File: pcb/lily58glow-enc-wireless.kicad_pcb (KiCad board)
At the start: 2 copper layers, 142.5 x 106.3 mm, 120 parts, among them J1 LED, J2 4PIN, P1 i2c_pin, P2 i2c_pin, P3 ICSP, P4 OLED, SW1 SW_PUSH, SW10 SW_PUSH, SW11 SW_PUSH, SW12 SW_PUSH, SW13 SW_PUSH, SW14 SW_PUSH, SW15 SW_PUSH, SW16 SW_PUSH, SW17 SW_PUSH, SW18 SW_PUSH, SW19 SW_PUSH, SW2 SW_PUSH, SW20 SW_PUSH, SW21 SW_PUSH, SW22 SW_PUSH, SW23 SW_PUSH, SW24 SW_PUSH, SW25 Rotary_Encoder_Switch, SW26 SW_PUSH, SW27 SW_PUSH, SW28 SW_PUSH, SW29 SW_PUSH, SW3 SW_PUSH, SW4 SW_PUSH, SW5 SW_PUSH, SW6 SW_PUSH, SW7 SW_PUSH, SW8 SW_PUSH, SW9 SW_PUSH, U1 ProMicro

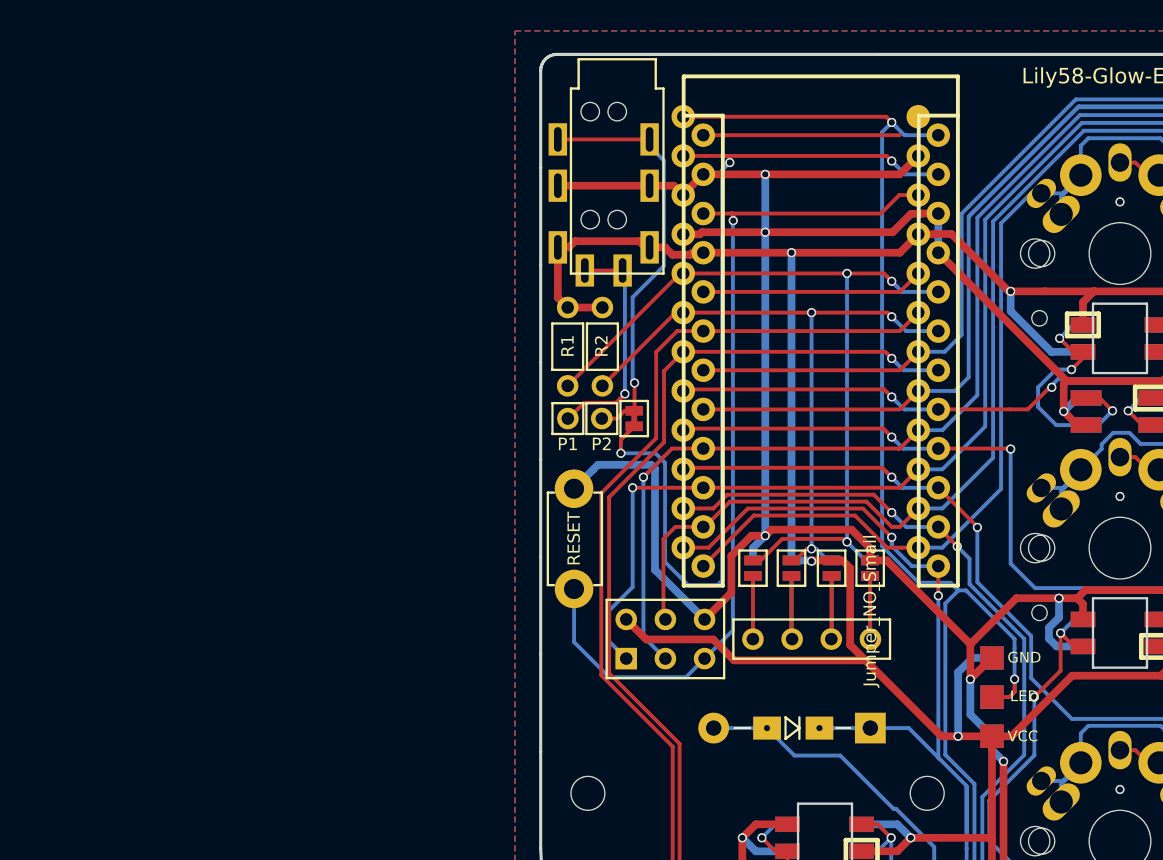
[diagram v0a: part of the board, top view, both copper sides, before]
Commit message: Updates to schematics
Might just scrap all of the traces and start from scratch...
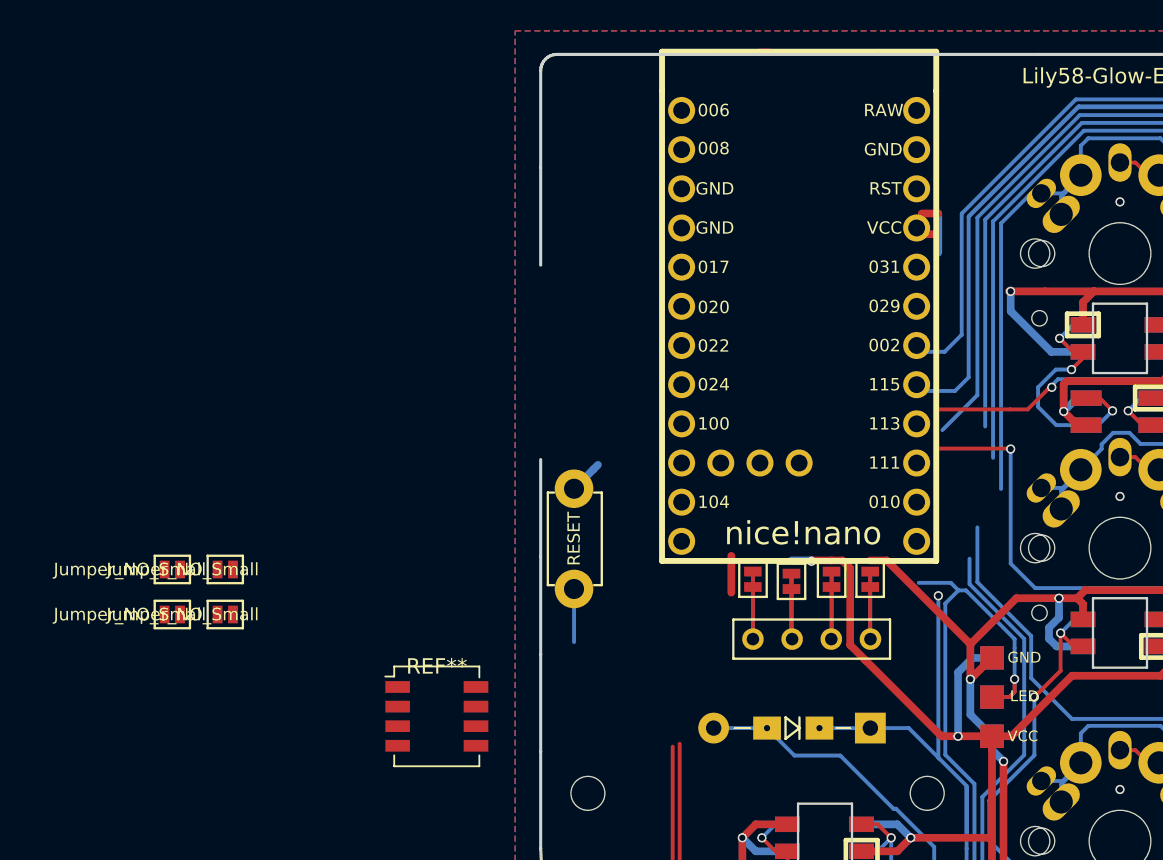
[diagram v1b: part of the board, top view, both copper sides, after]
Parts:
- removed J2: 4PIN, Lily58-footprint:MJ-4PP-9
- removed P1, P2: i2c_pin, Lily58-footprint:1pin_conn
- removed P3: ICSP, Lily58-footprint:ICSP
- removed R1, R2: R, Lily58-footprint:RESISTOR_mini
- removed W1: jumper, Lily58-footprint:jumper_data
- added REF**: SW_DIP_SPSTx04_Slide_Copal_CHS-04A_W5.08mm_P1.27mm_JPin, Button_Switch_SMD:SW_DIP_SPSTx04_Slide_Copal_CHS-04A_W5.08mm_P1.27mm_JPin, F.Cu at (76.2, 80.0)
- JP5, JP6, JP7, JP8: moved to F.Cu
- U1: footprint Lily58-footprint:ProMicro_rev2 -> nice-nano-kicad:nice_nano
- moved JP5 45.2 mm to (59.1, 70.5), turned to 0 degrees
- moved JP6 42.9 mm to (59.1, 73.4), turned to 0 degrees
- moved JP7 36.7 mm to (62.5, 70.5), turned to 0 degrees
- moved JP8 34.3 mm to (62.5, 73.4), turned to 0 degrees
- moved U1 1.78 mm to (99.7, 54.7), turned to -90 degrees
- moved JP3 0.85 mm to (99.2, 71.3)
- moved JP1 0.72 mm to (104.3, 71.1)
- moved JP2 0.72 mm to (101.8, 71.1)
- moved JP4 0.72 mm to (96.7, 71.1)
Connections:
- L1 pad 3: Net-(L1-Pad3) -> Net-(LEDDIP1-Pad8)
- L1 pad 4: VCC -> Net-(L1-Pad4)
- L10 pad 4: VCC -> Net-(L1-Pad4)
- L11 pad 4: VCC -> Net-(L1-Pad4)
- L12 pad 4: VCC -> Net-(L1-Pad4)
- L13 pad 4: VCC -> Net-(L1-Pad4)
- L14 pad 4: VCC -> Net-(L1-Pad4)
- L15 pad 4: VCC -> Net-(L1-Pad4)
- L16 pad 4: VCC -> Net-(L1-Pad4)
- L17 pad 4: VCC -> Net-(L1-Pad4)
- L18 pad 4: VCC -> Net-(L1-Pad4)
- L19 pad 4: VCC -> Net-(L1-Pad4)
- L2 pad 4: VCC -> Net-(L1-Pad4)
- L20 pad 4: VCC -> Net-(L1-Pad4)
- L21 pad 4: VCC -> Net-(L1-Pad4)
- L22 pad 4: VCC -> Net-(L1-Pad4)
- L23 pad 4: VCC -> Net-(L1-Pad4)
- L24 pad 4: VCC -> Net-(L1-Pad4)
- L25 pad 4: VCC -> Net-(L1-Pad4)
- L26 pad 4: VCC -> Net-(L1-Pad4)
- L27 pad 4: VCC -> Net-(L1-Pad4)
- L28 pad 4: VCC -> Net-(L1-Pad4)
- L29 pad 4: VCC -> Net-(L1-Pad4)
- L3 pad 4: VCC -> Net-(L1-Pad4)
- L30 pad 1: Net-(L30-Pad1) -> unconnected-(L30-Pad1)
- L30 pad 4: VCC -> Net-(L1-Pad4)
- L31 pad 1: Net-(L1-Pad3) -> unconnected-(L31-Pad1)
- L31 pad 4: VCC -> Net-(L31-Pad4)
- L32 pad 4: VCC -> Net-(L31-Pad4)
- L33 pad 4: VCC -> Net-(L31-Pad4)
- L34 pad 3: LED -> Net-(L34-Pad3)
- L34 pad 4: VCC -> Net-(L31-Pad4)
- L35 pad 4: VCC -> Net-(L31-Pad4)
- L36 pad 4: VCC -> Net-(L31-Pad4)
- L4 pad 4: VCC -> Net-(L1-Pad4)
- L5 pad 4: VCC -> Net-(L1-Pad4)
- L6 pad 4: VCC -> Net-(L1-Pad4)
- L7 pad 4: VCC -> Net-(L1-Pad4)
- L8 pad 4: VCC -> Net-(L1-Pad4)
- L9 pad 4: VCC -> Net-(L1-Pad4)
- U1 pad 1: LED -> Net-(LEDDIP1-Pad2)
- U1 pad 20: Net-(U1-Pad20) -> unconnected-(U1-Pad20)
- U1 pad 24: Net-(U1-Pad24) -> unconnected-(U1-Pad24)
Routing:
- net VCC: track 1045.9 -> 2.18 mm, vias 44 -> 0
- net Net-(L1-Pad4): track 0.00 -> 971.1 mm, vias 0 -> 43
- net GND: track 1095.1 -> 985.3 mm, vias 73 -> 69
- net DATA: track 60.9 -> 0.00 mm, vias 3 -> 0
- net RESET: track 57.5 -> 3.44 mm, vias 1 -> 0
- net SDA: track 53.7 -> 0.80 mm, vias 3 -> 0
- net LED: track 121.3 -> 71.3 mm, vias 5 -> 4
- net enc2: track 66.1 -> 19.0 mm
- net enc1: track 60.4 -> 14.0 mm, vias 1 -> 0
- net SCL: track 42.8 -> 0.51 mm, vias 3 -> 0
- net col3: track 300.2 -> 263.3 mm, vias 1 -> 0
- net col2: track 314.4 -> 281.4 mm, vias 1 -> 0
- net col4: track 291.3 -> 261.1 mm
- net Net-(J2-Pad3): track 26.7 -> 0.00 mm, vias 1 -> 0
- net col5: track 185.4 -> 162.3 mm
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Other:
- outline, holes or cut-outs redrawn

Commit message: Starting PCB from scratch, and making single sided boards
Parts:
- removed JP5, JP6, JP7, JP8: Jumper_NO_Small, Lily58-footprint:Jumper
- removed REF**: SW_DIP_SPSTx04_Slide_Copal_CHS-04A_W5.08mm_P1.27mm_JPin, Button_Switch_SMD:SW_DIP_SPSTx04_Slide_Copal_CHS-04A_W5.08mm_P1.27mm_JPin
- D1, D10, D11, D12, D13, D14, D15, D16, D17, D18, D19, D2, D20, D21, D22, D23, D24, D25, D27, D28, D29, D3, D4, D5, D6, D7, D8, D9: moved to F.Cu
- moved JP2 252.1 mm to (350.8, 31.4), turned to 0 degrees
- moved D26 238.7 mm to (333.1, 32.1), turned to 0 degrees
- moved L34 223.3 mm to (328.7, 36.5), turned to 0 degrees
- moved TH7 221.2 mm to (319.5, 60.7), turned to 0 degrees
- moved D25 220.5 mm to (316.8, 44.5), turned to 0 degrees
- moved L19 218.7 mm to (328.9, 46.3)
- moved L8 209.3 mm to (345.0, 32.8)
- moved TH2 201.3 mm to (308.8, 70.5)
- moved D27 200.9 mm to (309.3, 55.5), turned to 0 degrees
- moved J1 194.1 mm to (306.0, 69.1), turned to 0 degrees
- moved L2 181.7 mm to (321.1, 49.4), turned to 0 degrees
- moved L31 181.3 mm to (300.6, 81.2)
- moved L27 175.5 mm to (273.5, 102.0), turned to 0 degrees
- moved JP3 175.1 mm to (269.5, 112.0), turned to 0 degrees
- moved RSW1 175.1 mm to (255.3, 109.6), turned to 0 degrees
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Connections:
- L1 pad 3: Net-(LEDDIP1-Pad8) -> Net-(L1-Pad3)
- L1 pad 4: Net-(L1-Pad4) -> VCC
- L10 pad 4: Net-(L1-Pad4) -> VCC
- L11 pad 4: Net-(L1-Pad4) -> VCC
- L12 pad 4: Net-(L1-Pad4) -> VCC
- L13 pad 4: Net-(L1-Pad4) -> VCC
- L14 pad 4: Net-(L1-Pad4) -> VCC
- L15 pad 4: Net-(L1-Pad4) -> VCC
- L16 pad 4: Net-(L1-Pad4) -> VCC
- L17 pad 4: Net-(L1-Pad4) -> VCC
- L18 pad 4: Net-(L1-Pad4) -> VCC
- L19 pad 4: Net-(L1-Pad4) -> VCC
- L2 pad 4: Net-(L1-Pad4) -> VCC
- L20 pad 4: Net-(L1-Pad4) -> VCC
- L21 pad 4: Net-(L1-Pad4) -> VCC
- L22 pad 4: Net-(L1-Pad4) -> VCC
- L23 pad 4: Net-(L1-Pad4) -> VCC
- L24 pad 4: Net-(L1-Pad4) -> VCC
- L25 pad 4: Net-(L1-Pad4) -> VCC
- L26 pad 4: Net-(L1-Pad4) -> VCC
- L27 pad 4: Net-(L1-Pad4) -> VCC
- L28 pad 4: Net-(L1-Pad4) -> VCC
- L29 pad 4: Net-(L1-Pad4) -> VCC
- L3 pad 4: Net-(L1-Pad4) -> VCC
- L30 pad 4: Net-(L1-Pad4) -> VCC
- L31 pad 1: unconnected-(L31-Pad1) -> Net-(L1-Pad3)
- L31 pad 4: Net-(L31-Pad4) -> VCC
- L32 pad 4: Net-(L31-Pad4) -> VCC
- L33 pad 4: Net-(L31-Pad4) -> VCC
- L34 pad 3: Net-(L34-Pad3) -> LED
- L34 pad 4: Net-(L31-Pad4) -> VCC
- L35 pad 4: Net-(L31-Pad4) -> VCC
- L36 pad 4: Net-(L31-Pad4) -> VCC
- L4 pad 4: Net-(L1-Pad4) -> VCC
- L5 pad 4: Net-(L1-Pad4) -> VCC
- L6 pad 4: Net-(L1-Pad4) -> VCC
- L7 pad 4: Net-(L1-Pad4) -> VCC
- L8 pad 4: Net-(L1-Pad4) -> VCC
- L9 pad 4: Net-(L1-Pad4) -> VCC
- U1 pad 1: Net-(LEDDIP1-Pad2) -> LED
- U1 pad 23: GND -> -BATT
- U1 pad 24: unconnected-(U1-Pad24) -> +BATT
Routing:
- net GND: track 985.3 -> 0.00 mm, vias 69 -> 0
- net Net-(L1-Pad4): track 971.1 -> 0.00 mm, vias 43 -> 0
- net col1: track 367.7 -> 0.00 mm
- net col2: track 281.4 -> 0.00 mm
- net col3: track 263.3 -> 0.00 mm
- net col4: track 261.1 -> 0.00 mm
- net col0: track 256.5 -> 0.00 mm
- net col5: track 162.3 -> 0.00 mm, vias 2 -> 0
- net row3: track 161.2 -> 0.00 mm, vias 4 -> 0
- net row4: track 154.6 -> 0.00 mm, vias 4 -> 0
- net row2: track 146.5 -> 0.00 mm, vias 5 -> 0
- net row1: track 134.0 -> 0.00 mm, vias 6 -> 0
- net row0: track 132.5 -> 0.00 mm, vias 6 -> 0
- net LED: track 71.3 -> 0.00 mm, vias 4 -> 0
- net Net-(L27-Pad1): track 64.0 -> 0.00 mm, vias 3 -> 0
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- removed copper zone on B.Cu, net GND
- removed copper zone on F.Cu, net GND
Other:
- board outline removed
